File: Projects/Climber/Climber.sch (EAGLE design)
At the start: 3 parts, among them M1 VNH5019, M2 D36V6FX, U1 NRF52840-DONGLE

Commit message: New devices in Climber
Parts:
- added R1, R2: (no value), resistor:R-US_R0603
- added U$10: NET_CONN, NET_CONN:NET_CONN
- added U2: BSS138BKW, BSS138:BSS138BKW
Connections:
- new net GND: M1.GND, M2.GND, U$10.1, U$10.2, U1G$1.GND
- new net M1_CS: M1.CS
- new net M1_ENA/DIAGA: M1.ENA/DIAGA
- new net M1_ENB/DIAGB: M1.ENB/DIAGB
- new net M1_INA: M1.INA
- new net M1_INB: M1.INB
- new net M1_PWM: M1.PWM
- new net M1_VOUT: M1.VOUT
- new net NEO_HV: R2.1, U2.D
- new net NEO_LV: R1.1, U2.S
- new net VDD: M1.VDD, M2.VOUT, R1.2, U1G$1.VDDO
- new net VDD_5V: R2.2

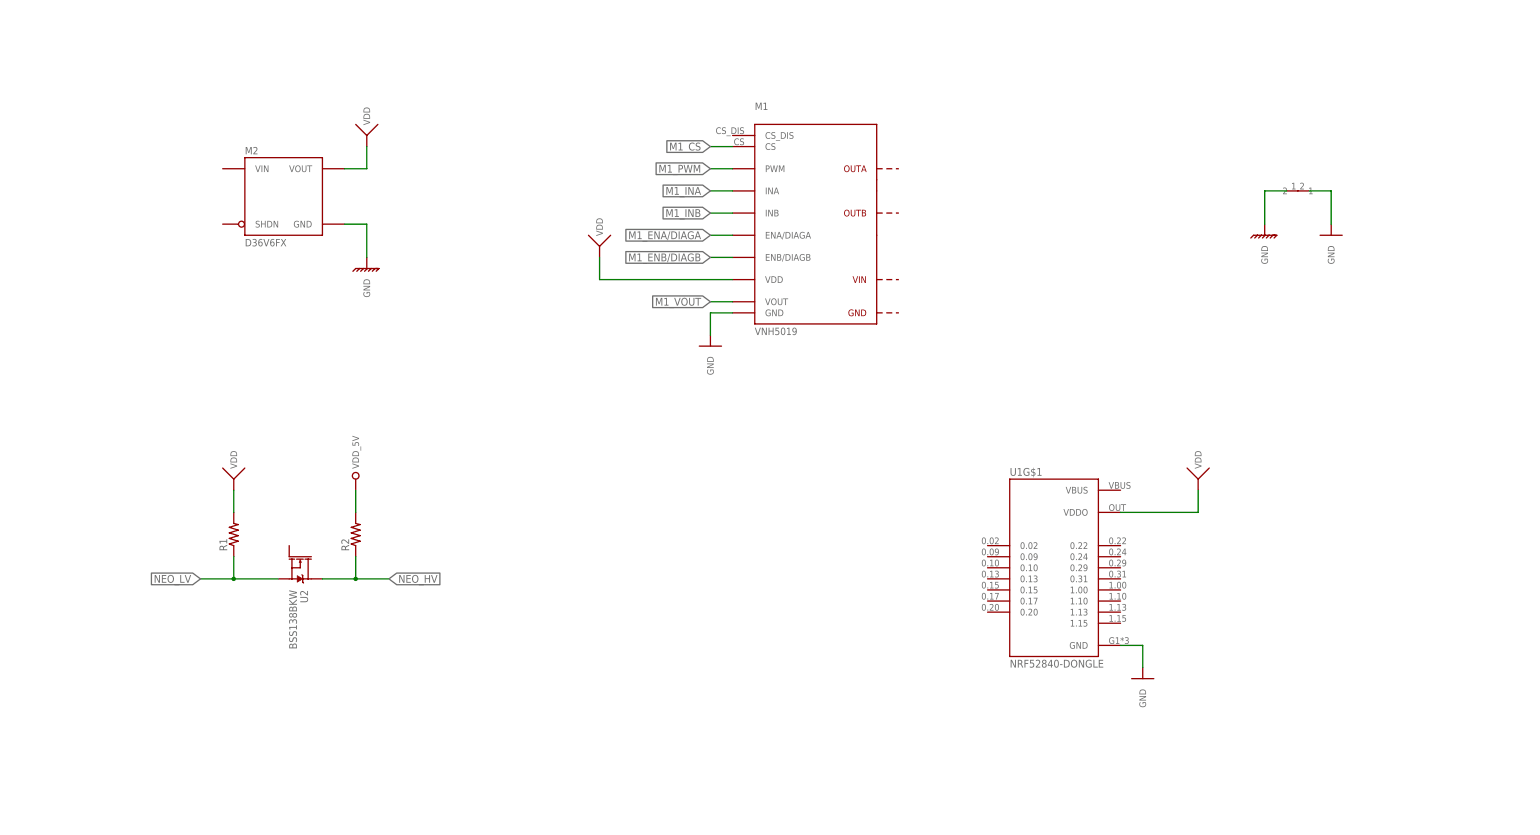
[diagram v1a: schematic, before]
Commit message: Added ZLL PCB, finished climber PCB
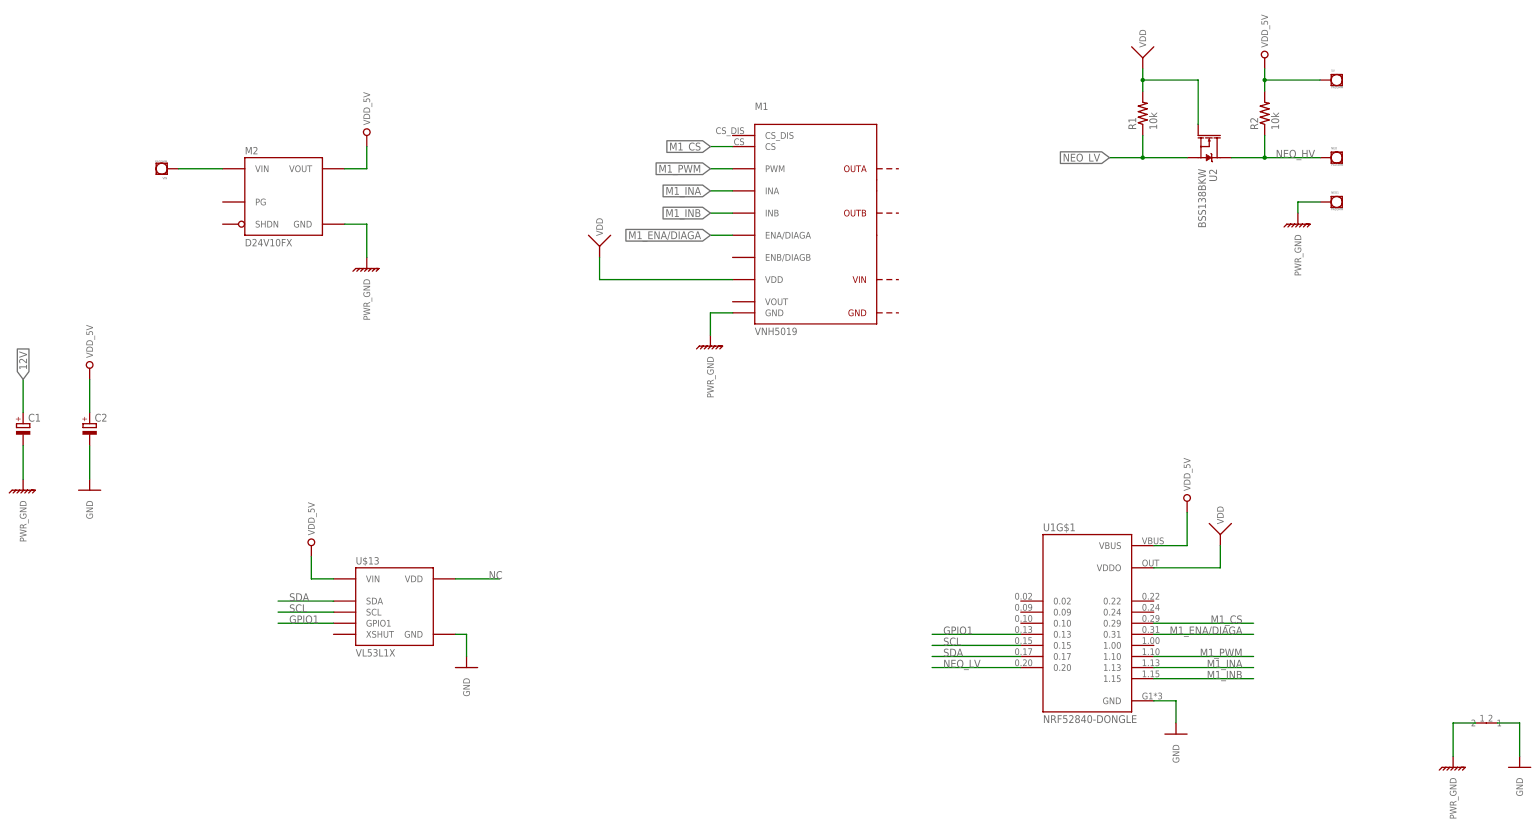
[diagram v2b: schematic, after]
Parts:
- added 5V, NEO, NEO1, VIN: PAD3MM, Exposed_pad:PAD3MM
- added C1, C2: (no value), resistor:CPOL-EUE5-4
- added U$13: VL53L1X, Pololu:VL53L1X
- M2: value D36V6FX -> D24V10FX; device Pololu:D36V6FX -> Pololu:D24V10FX
- R1, R2: value (none) -> 10k
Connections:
- removed net M1_ENB/DIAGB: M1.ENB/DIAGB
- removed net M1_VOUT: M1.VOUT
- new net 12V: C1.+, M2.VIN, VIN.1
- new net GPIO1: U$13.GPIO1, U1G$1.0.13
- new net NC: U$13.VDD
- new net PWR_GND: C1.-, M1.GND, M2.GND, NEO1.1, U$10.1
- new net SCL: U$13.SCL, U1G$1.0.15
- new net SDA: U$13.SDA, U1G$1.0.17
- net GND: now also C2.-, U$13.GND; no longer M1.GND, M2.GND, U$10.1
- net M1_CS: now also U1G$1.0.29
- net M1_ENA/DIAGA: now also U1G$1.0.31
- net M1_INA: now also U1G$1.1.13
- net M1_INB: now also U1G$1.1.15
- net M1_PWM: now also U1G$1.1.10
- net NEO_HV: now also NEO.1
- net NEO_LV: now also U1G$1.0.20
- net VDD: now also U2.G; no longer M2.VOUT
- net VDD_5V: now also 5V.1, C2.+, M2.VOUT, U$13.VIN, U1G$1.VBUS
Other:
- moved on the sheet: R1, R2, U1G$1, U2

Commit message: Order @ Boktech
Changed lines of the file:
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@@
 <pinref part="M1" gate="G$1" pin="VDD"/>
 <wire x1="-17.78" y1="22.86" x2="12.7" y2="22.86" width="0.1524" layer="91" grouprefs="MOTOR"/>
+<label x="-12.7" y="22.86" size="1.778" layer="95"/>
 </segment>
 <segment>
@@
 <wire x1="109.22" y1="-43.18" x2="124.46" y2="-43.18" width="0.1524" layer="91" grouprefs="MCU"/>
 <wire x1="124.46" y1="-43.18" x2="124.46" y2="-38.1" width="0.1524" layer="91" grouprefs="MCU"/>
+<label x="116.84" y="-43.18" size="1.778" layer="95"/>
 </segment>
 </net>
@@
 <pinref part="M2" gate="G$1" pin="VOUT"/>
 <pinref part="U$12" gate="G$1" pin="VDD_5V"/>
+<label x="-73.66" y="45.72" size="1.778" layer="95"/>
 </segment>
 <segment>
@@
 <wire x1="109.22" y1="-38.1" x2="116.84" y2="-38.1" width="0.1524" layer="91" grouprefs="MCU"/>
 <wire x1="116.84" y1="-38.1" x2="116.84" y2="-30.48" width="0.1524" layer="91" grouprefs="MCU"/>
+<label x="114.3" y="-38.1" size="1.778" layer="95"/>
 </segment>
 <segment>
@@
 <pinref part="M2" gate="G$1" pin="VIN"/>
 <wire x1="-114.3" y1="48.26" x2="-104.14" y2="48.26" width="0.1524" layer="91" grouprefs="VOLTAGE"/>
+<label x="-111.76" y="48.26" size="1.778" layer="95"/>
 </segment>
 <segment>
